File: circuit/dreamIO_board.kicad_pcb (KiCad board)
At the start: 2 copper layers, 60 x 60 mm, 78 parts, among them IC1 TPS61200, P1 BATT, P2 CONN_01X08, P3 CONN_01X08, P4 CONN_01X02, P5 CONN_01X06, P6 gnd_con, P9 PixelOut, SW1 SPDT, SW2 RESET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

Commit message: laid a few more traces. 50~ to go
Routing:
- net +3V3: track 46.2 -> 96.7 mm
- net RESET: track 7.24 -> 40.2 mm, vias 0 -> 2
- net GPIO14: track 5.22 -> 13.6 mm
- net ADC: track 5.22 -> 13.3 mm
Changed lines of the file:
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@@
   (general
     (links 193)
-    (no_connects 78)
+    (no_connects 56)
     (area 14.249999 13.649999 74.350001 73.750001)
     (thickness 1.6)
     (drawings 8)
-    (tracks 199)
+    (tracks 245)
     (zones 0)
     (modules 78)
@@
     (aux_axis_origin 0 0)
     (grid_origin 14.3 13.7)
-    (visible_elements FFFEFFFF)
+    (visible_elements FFFEFBFF)
     (pcbplotparams
       (layerselection 0x00030_80000001)
@@
   (segment (start 68.1 53.5) (end 68.1 50.5) (width 0.3) (layer F.Cu) (net 3))
   (segment (start 68.1 50.5) (end 68.9 49.7) (width 0.3) (layer F.Cu) (net 3))
-  (segment (start 66.10102 53.5) (end 66.10102 58.89898) (width 0.3) (layer F.Cu) (net 4) (status 400000))
-  (segment (start 37.55 62.95) (end 36.3501 62.95) (width 0.3) (layer F.Cu) (net 4) (status 800000))
-  (segment (start 37.8 62.7) (end 37.55 62.95) (width 0.3) (layer F.Cu) (net 4))
+  (segment (start 66.10102 53.5) (end 66.10102 58.89898) (width 0.1524) (layer F.Cu) (net 4))
+  (segment (start 66.10102 58.89898) (end 66.05 58.95) (width 0.1524) (layer F.Cu) (net 4))
+  (via (at 66.05 58.95) (size 0.6) (drill 0.4) (layers F.Cu B.Cu) (net 4))
+  (segment (start 66.05 58.95) (end 64.8 60.2) (width 0.1524) (layer B.Cu) (net 4))
+  (segment (start 64.8 60.2) (end 40.05 59.95) (width 0.1524) (layer B.Cu) (net 4))
+  (via (at 40.05 59.95) (size 0.6) (drill 0.4) (layers F.Cu B.Cu) (net 4))
+  (segment (start 40.05 59.95) (end 40.05 62.7) (width 0.1524) (layer F.Cu) (net 4))
+  (via (at 40.05 62.7) (size 0.6) (drill 0.4) (layers F.Cu B.Cu) (net 4))
+  (segment (start 40.05 62.7) (end 37.8 62.7) (width 0.1524) (layer B.Cu) (net 4))
   (via (at 37.8 62.7) (size 0.6) (drill 0.4) (layers F.Cu B.Cu) (net 4))
-  (segment (start 40.05 62.7) (end 37.8 62.7) (width 0.3) (layer B.Cu) (net 4))
-  (via (at 40.05 62.7) (size 0.6) (drill 0.4) (layers F.Cu B.Cu) (net 4))
-  (segment (start 40.05 59.95) (end 40.05 62.7) (width 0.3) (layer F.Cu) (net 4))
-  (via (at 40.05 59.95) (size 0.6) (drill 0.4) (layers F.Cu B.Cu) (net 4))
-  (segment (start 64.8 60.2) (end 40.05 59.95) (width 0.3) (layer B.Cu) (net 4))
-  (segment (start 66.05 58.95) (end 64.8 60.2) (width 0.3) (layer B.Cu) (net 4))
-  (via (at 66.05 58.95) (size 0.6) (drill 0.4) (layers F.Cu B.Cu) (net 4))
-  (segment (start 66.10102 58.89898) (end 66.05 58.95) (width 0.3) (layer F.Cu) (net 4))
+  (segment (start 37.8 62.7) (end 37.55 62.95) (width 0.1524) (layer F.Cu) (net 4))
+  (segment (start 37.55 62.95) (end 36.3501 62.95) (width 0.1524) (layer F.Cu) (net 4))
   (segment (start 62.9732 44.65178) (end 63.29812 44.65178) (width 0.16) (layer B.Cu) (net 4))
   (segment (start 59.0999 43.45) (end 62.8 43.45) (width 0.16) (layer B.Cu) (net 4))
@@
   (segment (start 60.0268 48.0233) (end 58.1001 49.95) (width 0.16) (layer B.Cu) (net 7))
   (segment (start 60.0268 46.64822) (end 60.0268 48.0233) (width 0.16) (layer B.Cu) (net 7))
+  (segment (start 66.2 62.0001) (end 67.8499 62.0001) (width 0.3) (layer F.Cu) (net 8))
+  (segment (start 67.8499 62.0001) (end 68.2 61.65) (width 0.3) (layer F.Cu) (net 8))
+  (segment (start 66.2 46.3001) (end 68.0499 46.3001) (width 0.3) (layer F.Cu) (net 8))
+  (segment (start 68.0499 46.3001) (end 68.2 46.15) (width 0.3) (layer F.Cu) (net 8))
+  (segment (start 66.3 31.0001) (end 67.8499 31.0001) (width 0.3) (layer F.Cu) (net 8))
+  (segment (start 67.8499 31.0001) (end 68.2 30.65) (width 0.3) (layer F.Cu) (net 8))
+  (segment (start 62.2 21.3999) (end 62.5001 21.7) (width 0.3) (layer F.Cu) (net 8))
+  (segment (start 62.2 19.8) (end 62.2 21.3999) (width 0.3) (layer F.Cu) (net 8))
+  (segment (start 46.95 19.8) (end 46.95 21.2499) (width 0.3) (layer F.Cu) (net 8))
+  (segment (start 46.95 21.2499) (end 47.3001 21.6) (width 0.3) (layer F.Cu) (net 8))
+  (segment (start 31.25 19.8) (end 31.25 21.4499) (width 0.3) (layer F.Cu) (net 8))
+  (segment (start 31.25 21.4499) (end 31.6001 21.8) (width 0.3) (layer F.Cu) (net 8))
+  (segment (start 20.4 25.75) (end 22.4499 25.75) (width 0.3) (layer F.Cu) (net 8))
+  (segment (start 22.4499 25.75) (end 22.8 25.3999) (width 0.3) (layer F.Cu) (net 8))
+  (segment (start 26.04956 25.49884) (end 28.29874 25.49884) (width 0.3) (layer F.Cu) (net 8))
+  (segment (start 28.29874 25.49884) (end 28.3 25.5001) (width 0.3) (layer F.Cu) (net 8))
+  (segment (start 26.04956 25.49884) (end 26.04956 33.90116) (width 0.3) (layer F.Cu) (net 8))
+  (segment (start 20.4 41.05) (end 21.7499 41.05) (width 0.3) (layer F.Cu) (net 8))
+  (segment (start 21.7499 41.05) (end 22.1 40.6999) (width 0.3) (layer F.Cu) (net 8))
+  (segment (start 20.4 56.75) (end 22.4499 56.75) (width 0.3) (layer F.Cu) (net 8))
+  (segment (start 22.4499 56.75) (end 22.8 56.3999) (width 0.3) (layer F.Cu) (net 8))
+  (segment (start 26.04956 53.49884) (end 26.04956 61.90116) (width 0.3) (layer F.Cu) (net 8))
+  (segment (start 26.04956 61.90116) (end 28.29874 61.90116) (width 0.3) (layer F.Cu) (net 8))
+  (segment (start 28.29874 61.90116) (end 28.3 61.8999) (width 0.3) (layer F.Cu) (net 8))
+  (segment (start 26.04956 61.90116) (end 26.04956 65.54966) (width 0.3) (layer F.Cu) (net 8))
+  (segment (start 26.04956 65.54966) (end 26.2999 65.8) (width 0.3) (layer F.Cu) (net 8))
+  (segment (start 26.2999 65.8) (end 26.2999 67.5499) (width 0.3) (layer F.Cu) (net 8))
+  (segment (start 26.2999 67.5499) (end 26.35 67.6) (width 0.3) (layer F.Cu) (net 8))
+  (segment (start 41.0999 65.8) (end 41.0999 66.8499) (width 0.3) (layer F.Cu) (net 8))
+  (segment (start 41.0999 66.8499) (end 41.85 67.6) (width 0.3) (layer F.Cu) (net 8))
+  (segment (start 56.9999 65.8) (end 56.9999 67.2499) (width 0.3) (layer F.Cu) (net 8))
+  (segment (start 56.9999 67.2499) (end 57.35 67.6) (width 0.3) (layer F.Cu) (net 8))
   (via (at 54.8 46.95) (size 0.6) (drill 0.4) (layers F.Cu B.Cu) (net 8))
   (segment (start 58.3 46.95) (end 54.8 46.95) (width 0.3) (layer B.Cu) (net 8))
@@
   (segment (start 38.85 16.6) (end 42.05 19.8) (width 0.25) (layer F.Cu) (net 16))
   (segment (start 68.25 56.75) (end 68.2 56.75) (width 0.3) (layer F.Cu) (net 20))
+  (segment (start 34.7499 62.95) (end 34.7499 57.6501) (width 0.1524) (layer F.Cu) (net 28))
+  (segment (start 34.7499 57.6501) (end 35.5 56.9) (width 0.1524) (layer F.Cu) (net 28))
+  (segment (start 34.7499 64.7) (end 34.7499 62.95) (width 0.1524) (layer F.Cu) (net 28))
   (segment (start 35.55 51.7) (end 35.55 56.85) (width 0.1524) (layer F.Cu) (net 28) (status 10))
   (segment (start 35.55 56.85) (end 35.5 56.9) (width 0.1524) (layer F.Cu) (net 28))
@@
   (segment (start 45.55 29.5001) (end 45.55 31.5) (width 0.1524) (layer F.Cu) (net 35))
   (segment (start 45.58 35.67) (end 45.55 35.7) (width 0.25) (layer F.Cu) (net 35) (status 30))
+  (segment (start 30.55044 53.49884) (end 30.55044 61.90116) (width 0.3) (layer F.Cu) (net 36))
   (segment (start 41.55 51.7) (end 41.55 56.85) (width 0.1524) (layer F.Cu) (net 36) (status 10))
   (segment (start 41.55 56.85) (end 41.5 56.9) (width 0.1524) (layer F.Cu) (net 36))
@@
   (segment (start 37.55 51.7) (end 37.55 56.85) (width 0.1524) (layer F.Cu) (net 48) (status 10))
   (segment (start 37.55 56.85) (end 37.5 56.9) (width 0.1524) (layer F.Cu) (net 48))
+  (segment (start 57.04956 62.90116) (end 57.04956 54.49884) (width 0.1524) (layer F.Cu) (net 49))
+  (via (at 33.55 54.95) (size 0.6) (drill 0.4) (layers F.Cu B.Cu) (net 49))
+  (segment (start 56.75116 54.49884) (end 55.3 55.95) (width 0.1524) (layer F.Cu) (net 49))
+  (via (at 55.3 55.95) (size 0.6) (drill 0.4) (layers F.Cu B.Cu) (net 49))
+  (segment (start 48.8 55.95) (end 55.3 55.95) (width 0.1524) (layer B.Cu) (net 49))
+  (segment (start 48.05 55.2) (end 48.8 55.95) (width 0.1524) (layer B.Cu) (net 49))
+  (segment (start 33.8 55.2) (end 48.05 55.2) (width 0.1524) (layer B.Cu) (net 49))
+  (segment (start 33.8 55.2) (end 33.55 54.95) (width 0.1524) (layer B.Cu) (net 49))
+  (segment (start 56.75116 54.49884) (end 57.04956 54.49884) (width 0.1524) (layer F.Cu) (net 49))
   (segment (start 33.5 56.9) (end 33.5 58.8499) (width 0.1524) (layer F.Cu) (net 49))
   (segment (start 33.5 58.8499) (end 33.55 58.8999) (width 0.1524) (layer F.Cu) (net 49))
-  (segment (start 33.55 51.7) (end 33.55 56.85) (width 0.1524) (layer F.Cu) (net 49) (status 10))
+  (segment (start 33.55 51.7) (end 33.55 54.95) (width 0.1524) (layer F.Cu) (net 49) (status 10))
+  (segment (start 33.55 54.95) (end 33.55 56.85) (width 0.1524) (layer F.Cu) (net 49) (status 10))
   (segment (start 33.55 56.85) (end 33.5 56.9) (width 0.1524) (layer F.Cu) (net 49))
   (zone (net 2) (net_name GND) (layer F.Cu) (hatch edge 0.508)

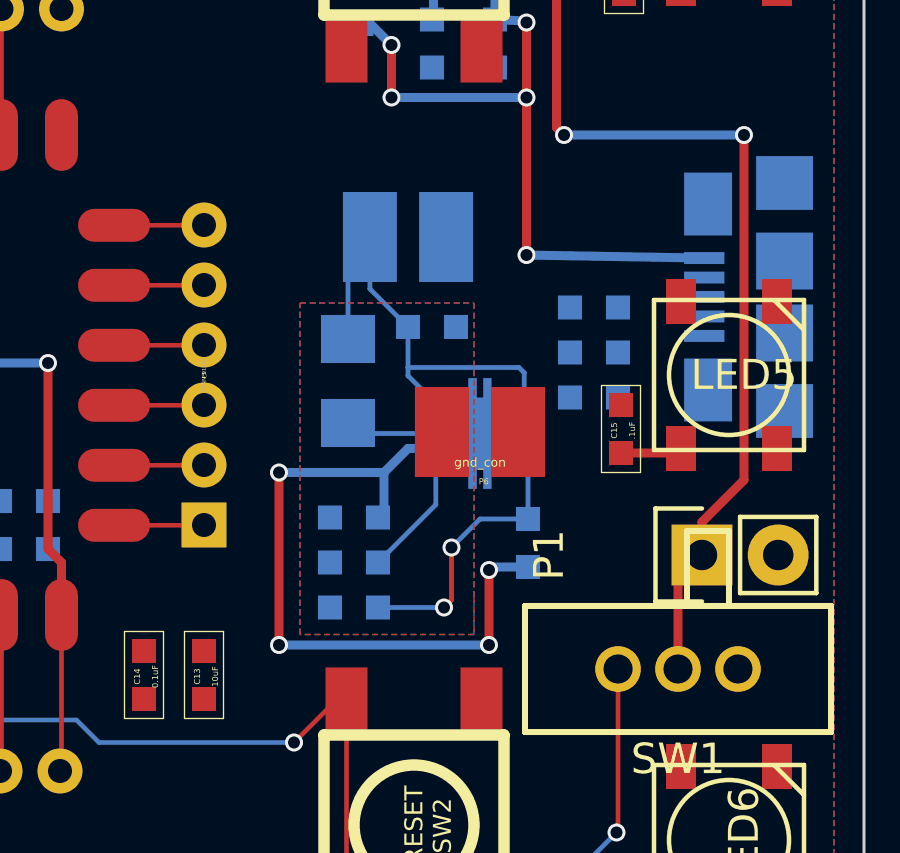
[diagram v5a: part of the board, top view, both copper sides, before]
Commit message: removed a (seemingly) extra capacitor from TPS section. Emulated the layout for TPS from datasheet. roughly 40 connections to go. wooooo!
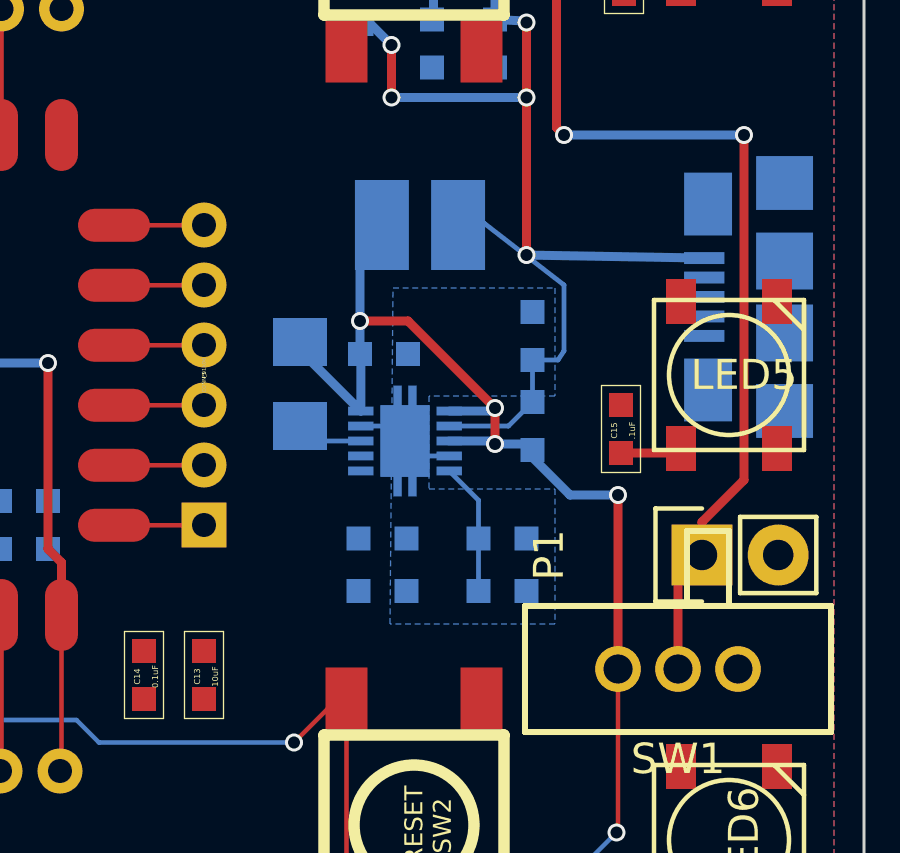
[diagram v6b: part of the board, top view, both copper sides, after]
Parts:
- removed C4: 0.1uF, kicad-libraries:0603
- removed P6: gnd_con, _connectors:_Solder_Pad2.54_2
- moved R7 5.46 mm to (62.2, 49.1), turned to 0 degrees
- moved R3 3.19 mm to (63.2, 45.4), turned to 90 degrees
- moved C5 2.63 mm to (58.2, 50.9), turned to 0 degrees
- moved IC1 2.51 mm to (59.0, 45.9)
- moved R6 2.26 mm to (63.2, 42.4), turned to 90 degrees
- moved C3 1.84 mm to (58.3, 43.0)
- moved R4 1.81 mm to (62.2, 50.9), turned to 180 degrees
- moved L1 1.60 mm to (55.5, 44.0)
- moved C6 1.24 mm to (58.2, 49.1), turned to 0 degrees
- moved P4 0.57 mm to (59.5, 38.7)
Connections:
- C3 pad 2: GNDA -> GND
- C5 pad 2: GNDA -> GND
- C6 pad 2: GNDA -> GND
- IC1 pad 4: GNDA -> GND
- R7 pad 2: GNDA -> GND
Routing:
- net +3V3: track 96.7 -> 73.0 mm, vias 5 -> 1
- net Net-(C3-Pad1): track 54.0 -> 70.7 mm, vias 4 -> 8
- net Net-(IC1-Pad7): track 0.67 -> 12.2 mm
- net Net-(IC1-Pad10): track 9.15 -> 4.41 mm, vias 2 -> 0
- net Net-(C6-Pad1): track 4.10 -> 0.00 mm
- net GND: track 9.43 -> 12.8 mm
- net Net-(IC1-Pad3): track 3.07 -> 2.23 mm
- removed copper zone on B.Cu, net GNDA
- removed copper zone on F.Cu, net GNDA

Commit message: finished board layout
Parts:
- moved R15 29.9 mm to (64.8, 58.7)
- moved R5 29.8 mm to (64.8, 57.2)
- moved C20 0.60 mm to (22.2, 57.2)
- moved R13 0.50 mm to (27.8, 62.7)
- moved R14 0.50 mm to (27.8, 24.7)
- moved L1 0.36 mm to (55.3, 43.7)
- moved C19 0.30 mm to (26.8, 65.8)
- moved C21 0.10 mm to (22.2, 41.5)
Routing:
- net +3V3: track 73.0 -> 326.8 mm, vias 1 -> 23
- net Net-(C3-Pad1): track 70.7 -> 36.4 mm, vias 8 -> 4
- net GPIO16: track 5.22 -> 39.1 mm, vias 0 -> 4
- net GPIO15: track 6.24 -> 30.3 mm, vias 0 -> 2
- net GPIO0: track 6.24 -> 30.3 mm, vias 0 -> 2
- net ADC: track 13.3 -> 36.6 mm, vias 0 -> 1
- net Net-(LED5-Pad2): track 0.05 -> 20.7 mm, vias 0 -> 6
- net Net-(LED7-Pad2): track 0.00 -> 17.2 mm, vias 0 -> 2
- net Net-(LED11-Pad2): track 0.00 -> 17.0 mm, vias 0 -> 4
- net Net-(LED4-Pad2): track 0.00 -> 16.5 mm, vias 0 -> 2
- net Net-(LED8-Pad2): track 0.00 -> 15.1 mm, vias 0 -> 2
- net Net-(LED10-Pad2): track 0.00 -> 13.7 mm, vias 0 -> 2
- net Net-(LED2-Pad2): track 0.00 -> 12.7 mm, vias 0 -> 2
- net Net-(LED3-Pad2): track 0.00 -> 11.7 mm
- net Net-(LED6-Pad2): track 0.00 -> 11.6 mm
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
